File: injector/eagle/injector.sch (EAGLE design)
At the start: 34 parts, among them J4 ICSP, U1 ATA6631, U2 ATMEGA328, U3 ATA6631, X1 16MHz

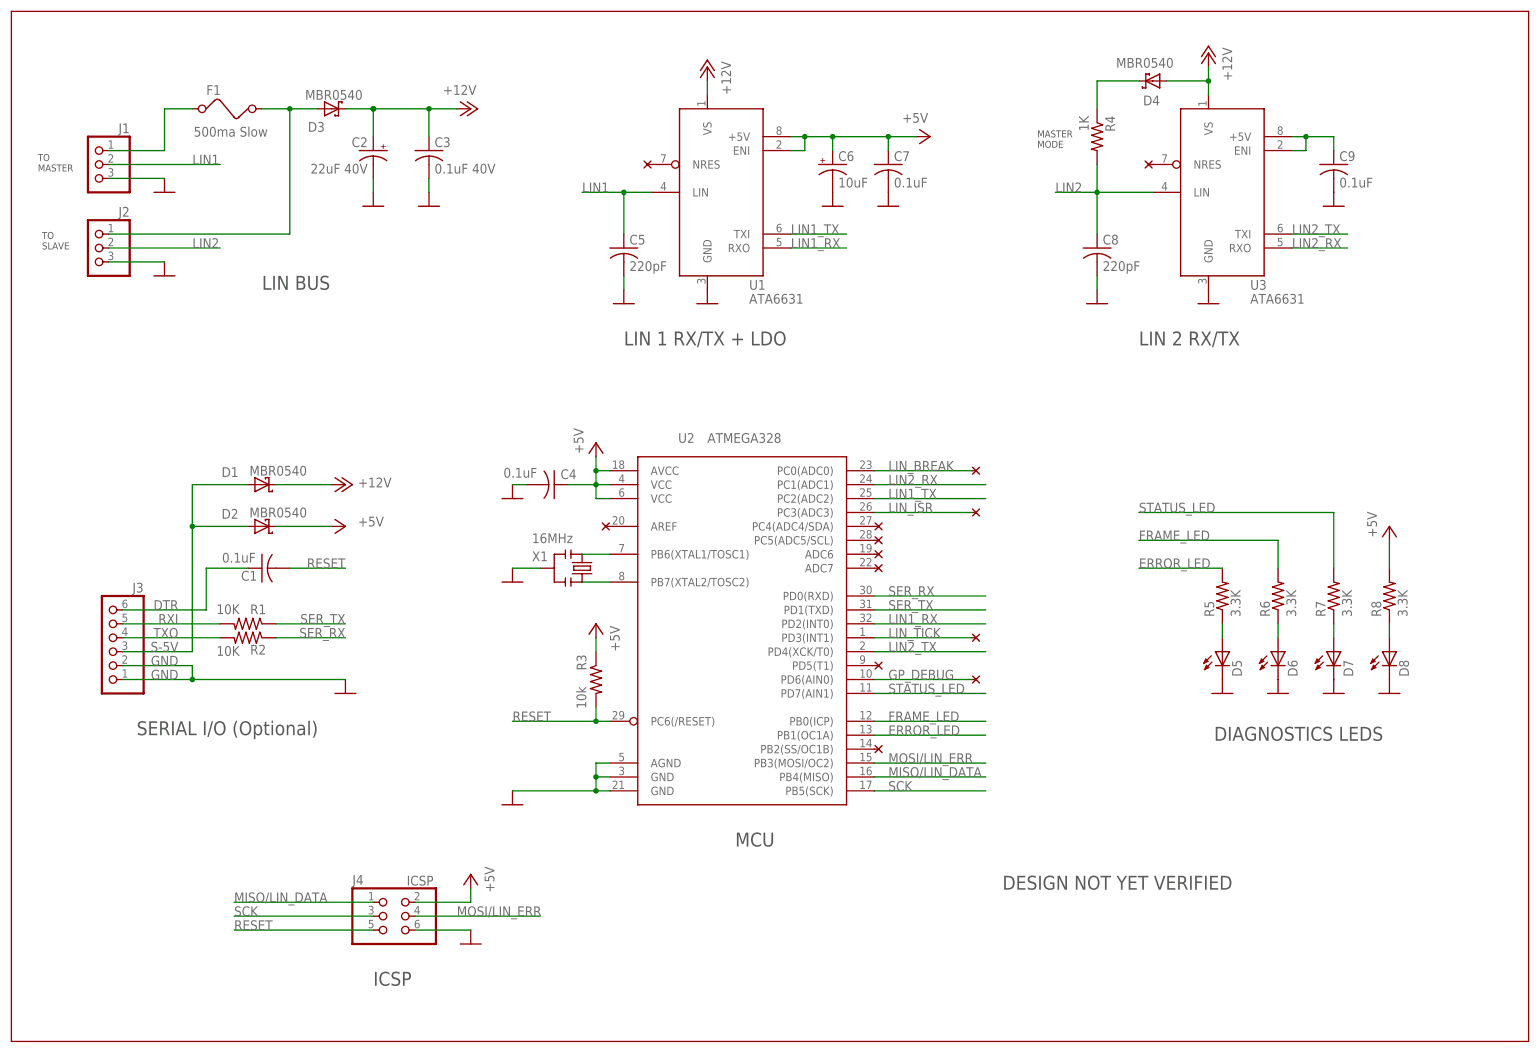
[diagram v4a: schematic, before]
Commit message: Tweaked schema's annotations, updated layout PDF.
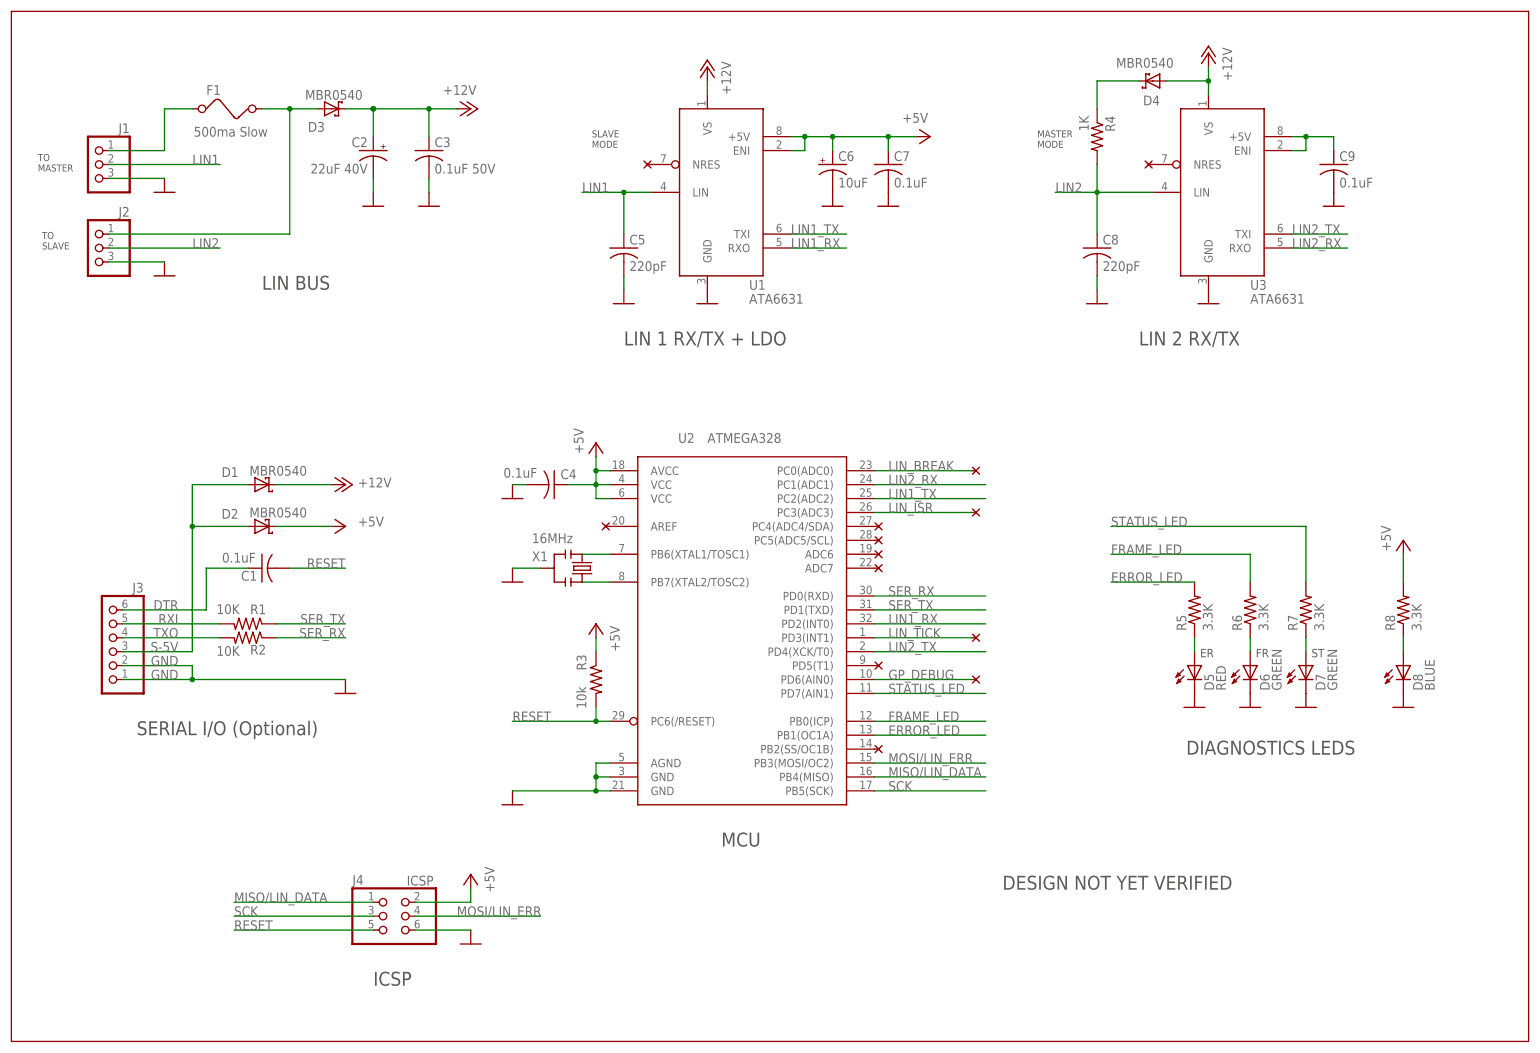
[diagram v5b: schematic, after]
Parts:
- C3: value 0.1uF 40V -> 0.1uF 50V
- D5: value (none) -> RED
- D6, D7: value (none) -> GREEN
- D8: value (none) -> BLUE
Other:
- note added: "ER"
- note added: "FR"
- note added: "SLAVE MODE"
- note added: "ST"
- moved on the sheet: D5, D6, D7, D8, R5, R6, R7, R8
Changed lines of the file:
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@@
 <part name="R5" library="injector" deviceset="R-US_" device="R0805" value="3.3K"/>
 <part name="R6" library="injector" deviceset="R-US_" device="R0805" value="3.3K"/>
-<part name="C3" library="injector" deviceset="C-US" device="C0805" value="0.1uF 40V"/>
+<part name="C3" library="injector" deviceset="C-US" device="C0805" value="0.1uF 50V"/>
 <part name="C2" library="injector" deviceset="CPOL-US" device="UD-6,3X5,8" value="22uF 40V"/>
 <part name="J1" library="injector" deviceset="PINHD-1X3" device=""/>
@@
 <part name="U$10" library="injector" deviceset="NC" device=""/>
 <part name="U$11" library="injector" deviceset="NC" device=""/>
-<part name="D5" library="injector" deviceset="LED" device=""/>
-<part name="D6" library="injector" deviceset="LED" device=""/>
+<part name="D5" library="injector" deviceset="LED" device="" value="RED"/>
+<part name="D6" library="injector" deviceset="LED" device="" value="GREEN"/>
 <part name="U$13" library="injector" deviceset="DOCFIELD" device=""/>
 <part name="C4" library="injector" deviceset="C-US" device="C0805" value="0.1uF"/>
@@
 <part name="U$12" library="injector" deviceset="NC" device=""/>
 <part name="U$14" library="injector" deviceset="NC" device=""/>
-<part name="D7" library="injector" deviceset="LED" device=""/>
-<part name="D8" library="injector" deviceset="LED" device=""/>
+<part name="D7" library="injector" deviceset="LED" device="" value="GREEN"/>
+<part name="D8" library="injector" deviceset="LED" device="" value="BLUE"/>
 <part name="GND1" library="injector" deviceset="GND" device=""/>
 <part name="GND16" library="injector" deviceset="GND" device=""/>
@@
 <wire x1="33.02" y1="25.4" x2="309.88" y2="25.4" width="0.1524" layer="94"/>
 <text x="78.74" y="162.56" size="2.54" layer="97">LIN BUS</text>
-<text x="252.476" y="80.264" size="2.54" layer="97">DIAGNOSTICS LEDS</text>
+<text x="247.396" y="77.724" size="2.54" layer="97">DIAGNOSTICS LEDS</text>
 <text x="99.06" y="35.56" size="2.54" layer="97">ICSP</text>
 <text x="144.78" y="152.4" size="2.54" layer="97">LIN 1 RX/TX + LDO</text>
 <text x="238.76" y="152.4" size="2.54" layer="97">LIN 2 RX/TX</text>
-<text x="165.1" y="60.96" size="2.54" layer="97">MCU</text>
+<text x="162.56" y="60.96" size="2.54" layer="97">MCU</text>
 <text x="55.88" y="81.28" size="2.54" layer="97">SERIAL I/O (Optional)</text>
 <wire x1="33.02" y1="25.4" x2="33.02" y2="213.36" width="0.1524" layer="94"/>
@@
 <text x="38.608" y="169.926" size="1.27" layer="97">TO
 SLAVE</text>
+<text x="249.936" y="95.504" size="1.524" layer="97">ER</text>
+<text x="260.096" y="95.504" size="1.524" layer="97">FR</text>
+<text x="270.256" y="95.504" size="1.524" layer="97">ST</text>
+<text x="138.938" y="188.468" size="1.27" layer="97">SLAVE
+MODE</text>
 </plain>
 <instances>
-<instance part="R5" gate="G$1" x="254" y="106.68" rot="R90"/>
-<instance part="R6" gate="G$1" x="264.16" y="106.68" rot="R90"/>
+<instance part="R5" gate="G$1" x="248.92" y="104.14" rot="R90"/>
+<instance part="R6" gate="G$1" x="259.08" y="104.14" rot="R90"/>
 <instance part="C3" gate="G$1" x="109.22" y="187.96"/>
 <instance part="C2" gate="G$1" x="99.06" y="187.96" rot="MR0"/>
@@
 <attribute name="VALUE" x="86.614" y="197.231" size="1.778" layer="96"/>
 </instance>
-<instance part="GND3" gate="1" x="254" y="88.9"/>
+<instance part="GND3" gate="1" x="248.92" y="86.36"/>
 <instance part="GND7" gate="1" x="60.96" y="180.34"/>
 <instance part="GND8" gate="1" x="109.22" y="177.8"/>
@@
 <attribute name="VALUE" x="66.294" y="190.5" size="1.778" layer="96"/>
 </instance>
-<instance part="GND2" gate="1" x="264.16" y="88.9"/>
+<instance part="GND2" gate="1" x="259.08" y="86.36"/>
 <instance part="J4" gate="A" x="101.6" y="48.26" smashed="yes">
 <attribute name="NAME" x="95.25" y="53.975" size="1.778" layer="95"/>
@@
 <instance part="U$10" gate="G$1" x="142.24" y="119.38"/>
 <instance part="U$11" gate="G$1" x="190.5" y="78.74" rot="R180"/>
-<instance part="D5" gate="G$1" x="254" y="96.52"/>
-<instance part="D6" gate="G$1" x="264.16" y="96.52"/>
+<instance part="D5" gate="G$1" x="248.92" y="93.98" smashed="yes">
+<attribute name="NAME" x="252.476" y="89.408" size="1.778" layer="95" rot="R90"/>
+<attribute name="VALUE" x="254.635" y="89.408" size="1.778" layer="96" rot="R90"/>
+</instance>
+<instance part="D6" gate="G$1" x="259.08" y="93.98" smashed="yes">
+<attribute name="NAME" x="262.636" y="89.408" size="1.778" layer="95" rot="R90"/>
+<attribute name="VALUE" x="264.795" y="89.408" size="1.778" layer="96" rot="R90"/>
+</instance>
 <instance part="U$13" gate="G$1" x="208.28" y="25.4"/>
 <instance part="C4" gate="G$1" x="132.08" y="127" smashed="yes" rot="R270">
@@
 <instance part="U$12" gate="G$1" x="190.5" y="93.98" rot="R180"/>
 <instance part="U$14" gate="G$1" x="208.28" y="91.44" rot="R180"/>
-<instance part="D7" gate="G$1" x="274.32" y="96.52"/>
-<instance part="D8" gate="G$1" x="284.48" y="96.52"/>
-<instance part="GND1" gate="1" x="274.32" y="88.9"/>
-<instance part="GND16" gate="1" x="284.48" y="88.9"/>
-<instance part="R8" gate="G$1" x="284.48" y="106.68" rot="R90"/>
-<instance part="R7" gate="G$1" x="274.32" y="106.68" rot="R90"/>
-<instance part="P+8" gate="1" x="284.48" y="119.38" smashed="yes">
-<attribute name="VALUE" x="282.194" y="117.348" size="1.778" layer="96" rot="R90"/>
+<instance part="D7" gate="G$1" x="269.24" y="93.98" smashed="yes">
+<attribute name="NAME" x="272.796" y="89.408" size="1.778" layer="95" rot="R90"/>
+<attribute name="VALUE" x="274.955" y="89.408" size="1.778" layer="96" rot="R90"/>
+</instance>
+<instance part="D8" gate="G$1" x="287.02" y="93.98" smashed="yes">
+<attribute name="NAME" x="290.576" y="89.408" size="1.778" layer="95" rot="R90"/>
+<attribute name="VALUE" x="292.735" y="89.408" size="1.778" layer="96" rot="R90"/>
+</instance>
+<instance part="GND1" gate="1" x="269.24" y="86.36"/>
+<instance part="GND16" gate="1" x="287.02" y="86.36"/>
+<instance part="R8" gate="G$1" x="287.02" y="104.14" rot="R90"/>
+<instance part="R7" gate="G$1" x="269.24" y="104.14" rot="R90"/>
+<instance part="P+8" gate="1" x="287.02" y="116.84" smashed="yes">
+<attribute name="VALUE" x="284.734" y="114.808" size="1.778" layer="96" rot="R90"/>
 </instance>
 </instances>
@@
 <segment>
 <pinref part="R6" gate="G$1" pin="1"/>
-<wire x1="264.16" y1="99.06" x2="264.16" y2="101.6" width="0.1524" layer="91"/>
+<wire x1="259.08" y1="96.52" x2="259.08" y2="99.06" width="0.1524" layer="91"/>
 <pinref part="D6" gate="G$1" pin="A"/>
 </segment>
@@
 <segment>
 <pinref part="R5" gate="G$1" pin="1"/>
-<wire x1="254" y1="101.6" x2="254" y2="99.06" width="0.1524" layer="91"/>
+<wire x1="248.92" y1="99.06" x2="248.92" y2="96.52" width="0.1524" layer="91"/>
 <pinref part="D5" gate="G$1" pin="A"/>
 </segment>
@@
 <pinref part="P+8" gate="1" pin="+5V"/>
 <pinref part="R8" gate="G$1" pin="2"/>
-<wire x1="284.48" y1="116.84" x2="284.48" y2="111.76" width="0.1524" layer="91"/>
+<wire x1="287.02" y1="114.3" x2="287.02" y2="109.22" width="0.1524" layer="91"/>
 </segment>
 </net>
@@
 <segment>
 <pinref part="R5" gate="G$1" pin="2"/>
-<wire x1="238.76" y1="111.76" x2="254" y2="111.76" width="0.1524" layer="91"/>
-<label x="238.76" y="111.76" size="1.778" layer="95"/>
+<wire x1="233.68" y1="109.22" x2="248.92" y2="109.22" width="0.1524" layer="91"/>
+<label x="233.68" y="109.22" size="1.778" layer="95"/>
 </segment>
 <segment>
@@
 <segment>
 <pinref part="R6" gate="G$1" pin="2"/>
-<wire x1="238.76" y1="116.84" x2="264.16" y2="116.84" width="0.1524" layer="91"/>
-<wire x1="264.16" y1="116.84" x2="264.16" y2="111.76" width="0.1524" layer="91"/>
-<label x="238.76" y="116.84" size="1.778" layer="95"/>
+<wire x1="233.68" y1="114.3" x2="259.08" y2="114.3" width="0.1524" layer="91"/>
+<wire x1="259.08" y1="114.3" x2="259.08" y2="109.22" width="0.1524" layer="91"/>
+<label x="233.68" y="114.3" size="1.778" layer="95"/>
 </segment>
 <segment>
@@
 <pinref part="R7" gate="G$1" pin="1"/>
 <pinref part="D7" gate="G$1" pin="A"/>
-<wire x1="274.32" y1="101.6" x2="274.32" y2="99.06" width="0.1524" layer="91"/>
+<wire x1="269.24" y1="99.06" x2="269.24" y2="96.52" width="0.1524" layer="91"/>
 </segment>
 </net>
@@
 <pinref part="R8" gate="G$1" pin="1"/>
 <pinref part="D8" gate="G$1" pin="A"/>
-<wire x1="284.48" y1="101.6" x2="284.48" y2="99.06" width="0.1524" layer="91"/>
+<wire x1="287.02" y1="99.06" x2="287.02" y2="96.52" width="0.1524" layer="91"/>
 </segment>
 </net>
@@
 <segment>
 <pinref part="R7" gate="G$1" pin="2"/>
-<wire x1="274.32" y1="111.76" x2="274.32" y2="121.92" width="0.1524" layer="91"/>
-<wire x1="274.32" y1="121.92" x2="238.76" y2="121.92" width="0.1524" layer="91"/>
-<label x="238.76" y="121.92" size="1.778" layer="95"/>
-</segment>
-</net>
+<wire x1="269.24" y1="109.22" x2="269.24" y2="119.38" width="0.1524" layer="91"/>
+<wire x1="269.24" y1="119.38" x2="233.68" y2="119.38" width="0.1524" layer="91"/>
+<label x="233.68" y="119.38" size="1.778" layer="95"/>
+</segment>
+</net>

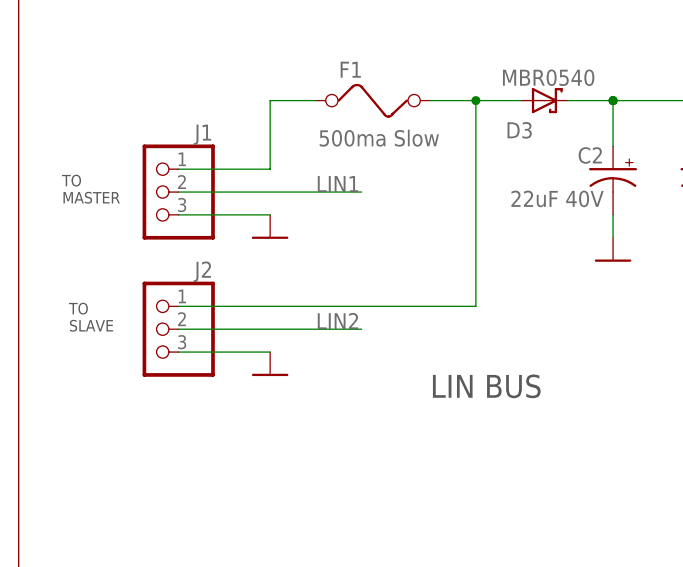
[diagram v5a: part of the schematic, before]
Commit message: Swapped the LIN and GND pins in the two 3 pin linbus headers. This will make this board consistent with the Beeper and Analyzer boards and with the P981 wiring.
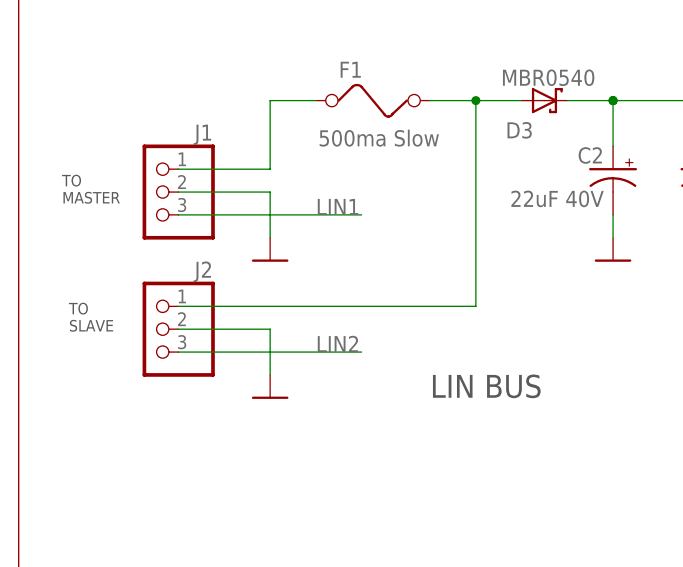
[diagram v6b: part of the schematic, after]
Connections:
- net GND: now also J1.2, J2.2; no longer J1.3, J2.3
- net LIN1: now also J1.3; no longer J1.2
- net LIN2: now also J2.3; no longer J2.2
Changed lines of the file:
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@@
 </instance>
 <instance part="GND3" gate="1" x="248.92" y="86.36"/>
-<instance part="GND7" gate="1" x="60.96" y="180.34"/>
+<instance part="GND7" gate="1" x="60.96" y="177.8"/>
 <instance part="GND8" gate="1" x="109.22" y="177.8"/>
 <instance part="GND9" gate="1" x="99.06" y="177.8"/>
@@
 <instance part="J2" gate="A" x="48.26" y="170.18" rot="MR0"/>
 <instance part="GND15" gate="1" x="251.46" y="160.02"/>
-<instance part="GND19" gate="1" x="60.96" y="165.1"/>
+<instance part="GND19" gate="1" x="60.96" y="162.56"/>
 <instance part="P+2" gate="1" x="116.84" y="195.58" rot="R270"/>
 <instance part="C9" gate="G$1" x="274.32" y="185.42"/>
@@
 <net name="GND" class="0">
 <segment>
-<pinref part="J1" gate="A" pin="3"/>
-<wire x1="50.8" y1="182.88" x2="60.96" y2="182.88" width="0.1524" layer="91"/>
-<pinref part="GND7" gate="1" pin="GND"/>
-</segment>
-<segment>
 <pinref part="C3" gate="G$1" pin="2"/>
 <pinref part="GND8" gate="1" pin="GND"/>
@@
 <pinref part="U1" gate="G$1" pin="GND"/>
 <pinref part="GND10" gate="1" pin="GND"/>
-</segment>
-<segment>
-<pinref part="J2" gate="A" pin="3"/>
-<wire x1="50.8" y1="167.64" x2="60.96" y2="167.64" width="0.1524" layer="91"/>
-<pinref part="GND19" gate="1" pin="GND"/>
 </segment>
 <segment>
@@
 <pinref part="GND16" gate="1" pin="GND"/>
 </segment>
+<segment>
+<pinref part="J1" gate="A" pin="2"/>
+<pinref part="GND7" gate="1" pin="GND"/>
+<wire x1="50.8" y1="185.42" x2="60.96" y2="185.42" width="0.1524" layer="91"/>
+<wire x1="60.96" y1="185.42" x2="60.96" y2="180.34" width="0.1524" layer="91"/>
+</segment>
+<segment>
+<pinref part="J2" gate="A" pin="2"/>
+<wire x1="50.8" y1="170.18" x2="60.96" y2="170.18" width="0.1524" layer="91"/>
+<pinref part="GND19" gate="1" pin="GND"/>
+<wire x1="60.96" y1="170.18" x2="60.96" y2="165.1" width="0.1524" layer="91"/>
+</segment>
 </net>
 <net name="N$3" class="0">
@@
 </net>
 <net name="LIN1" class="0">
-<segment>
-<pinref part="J1" gate="A" pin="2"/>
-<label x="66.04" y="185.42" size="1.778" layer="95"/>
-<wire x1="50.8" y1="185.42" x2="71.12" y2="185.42" width="0.1524" layer="91"/>
-</segment>
 <segment>
 <pinref part="U1" gate="G$1" pin="LIN"/>
@@
 <junction x="144.78" y="180.34"/>
 <label x="137.16" y="180.34" size="1.778" layer="95"/>
+</segment>
+<segment>
+<pinref part="J1" gate="A" pin="3"/>
+<wire x1="50.8" y1="182.88" x2="71.12" y2="182.88" width="0.1524" layer="91"/>
+<label x="66.04" y="182.88" size="1.778" layer="95"/>
 </segment>
 </net>
@@
 <net name="LIN2" class="0">
 <segment>
-<pinref part="J2" gate="A" pin="2"/>
-<wire x1="50.8" y1="170.18" x2="71.12" y2="170.18" width="0.1524" layer="91"/>
-<label x="66.04" y="170.18" size="1.778" layer="95"/>
-</segment>
-<segment>
 <pinref part="R4" gate="G$1" pin="2"/>
 <pinref part="C8" gate="G$1" pin="1"/>
@@
 <label x="223.52" y="180.34" size="1.778" layer="95"/>
 </segment>
-</net>
+<segment>
+<pinref part="J2" gate="A" pin="3"/>
+<wire x1="50.8" y1="167.64" x2="71.12" y2="167.64" width="0.1524" layer="91"/>
+<label x="66.04" y="167.64" size="1.778" layer="95"/>
+</segment>
+</net>
